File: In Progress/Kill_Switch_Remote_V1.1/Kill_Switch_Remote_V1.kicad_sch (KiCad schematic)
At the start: 56 parts, among them J1 USB_B_Micro, J2 S2B-PH-K-S(LF)(SN), J3 U.FL-R-SMT-1(10), Q2 UMH3N, SW4 AS11CH, U1 ESP32-PICO-MINI-02, U2 CP2102N-A02-GQFN28, U3 LP5912-3.3DRV, U4 MCP73871-2CC-Custom, U5 RFM95W-915S2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

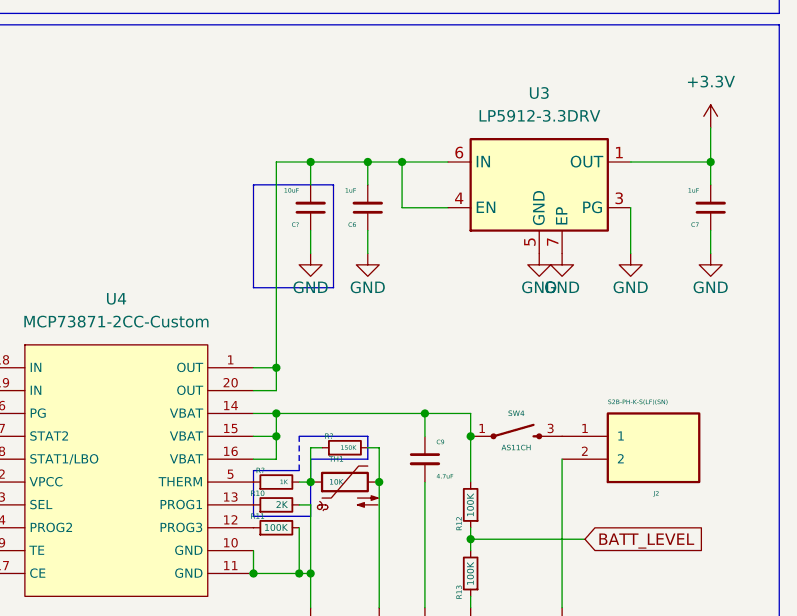
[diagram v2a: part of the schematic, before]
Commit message: changed folder name
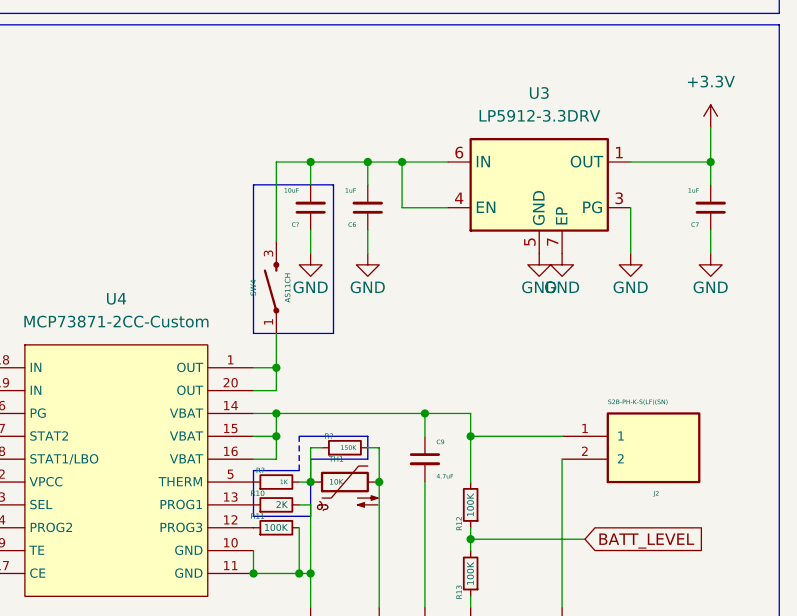
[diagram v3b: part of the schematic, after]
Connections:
- net at J2.1: now also C9.1, R12.2, U4.14 (VBAT), U4.15 (VBAT), U4.16 (VBAT); no longer SW4.3
- net at C6.2, C?.2, U3.4 (EN)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: now also SW4.3; no longer U4.1 (OUT), U4.20 (OUT)
- new net: SW4.1, U4.1 (OUT), U4.20 (OUT)
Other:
- moved on the sheet: SW4
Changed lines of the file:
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@@
   (junction (at 48.26 21.59) (diameter 0) (color 0 0 0 0)
   )
-  (junction (at 248.92 134.62) (diameter 0) (color 0 0 0 0)
-  )
   (junction (at 172.72 127) (diameter 0) (color 0 0 0 0)
   )
@@
   (junction (at 231.14 149.86) (diameter 0) (color 0 0 0 0)
   )
+  (junction (at 248.92 134.62) (diameter 0) (color 0 0 0 0)
+  )
   (junction (at 227.33 127) (diameter 0) (color 0 0 0 0)
   )
@@
     (stroke (width 0) (type default) (color 0 0 0 0))
   )
-  (polyline (pts (xy 233.68 106.68) (xy 233.68 118.11))
+  (polyline (pts (xy 233.68 106.68) (xy 233.68 123.19))
     (stroke (width 0) (type default) (color 0 0 0 0))
   )
@@
     (stroke (width 0) (type default) (color 0 0 0 0))
   )
+  (wire (pts (xy 248.92 134.62) (xy 248.92 139.7))
+    (stroke (width 0) (type default) (color 0 0 0 0))
+  )
   (wire (pts (xy 220.98 59.69) (xy 220.98 60.96))
     (stroke (width 0) (type default) (color 0 0 0 0))
@@
     (stroke (width 0) (type default) (color 0 0 0 0))
   )
-  (polyline (pts (xy 224.79 106.68) (xy 224.79 118.11))
+  (polyline (pts (xy 224.79 106.68) (xy 224.79 123.19))
     (stroke (width 0) (type default) (color 0 0 0 0))
   )
@@
     (stroke (width 0) (type default) (color 0 0 0 0))
   )
-  (wire (pts (xy 248.92 134.62) (xy 248.92 139.7))
-    (stroke (width 0) (type default) (color 0 0 0 0))
-  )
   (wire (pts (xy 179.07 142.24) (xy 179.07 151.13))
     (stroke (width 0) (type default) (color 0 0 0 0))
@@
     (stroke (width 0) (type default) (color 0 0 0 0))
   )
-  (wire (pts (xy 227.33 104.14) (xy 227.33 127))
+  (wire (pts (xy 227.33 104.14) (xy 227.33 113.03))
     (stroke (width 0) (type default) (color 0 0 0 0))
   )
@@
     (stroke (width 0) (type default) (color 0 0 0 0))
   )
+  (wire (pts (xy 248.92 134.62) (xy 259.08 134.62))
+    (stroke (width 0) (type default) (color 0 0 0 0))
+  )
   (wire (pts (xy 83.82 21.59) (xy 83.82 26.67))
     (stroke (width 0) (type default) (color 0 0 0 0))
@@
     (stroke (width 0) (type default) (color 0 0 0 0))
   )
+  (wire (pts (xy 227.33 123.19) (xy 227.33 127))
+    (stroke (width 0) (type default) (color 0 0 0 0))
+  )
   (wire (pts (xy 17.78 68.58) (xy 20.32 68.58))
     (stroke (width 0) (type default) (color 0 0 0 0))
@@
     (stroke (width 0) (type default) (color 0 0 0 0))
   )
-  (polyline (pts (xy 233.68 118.11) (xy 224.79 118.11))
+  (polyline (pts (xy 233.68 123.19) (xy 224.79 123.19))
     (stroke (width 0) (type default) (color 0 0 0 0))
   )
@@
     (pin "1")
   )
-  (symbol (lib_id "Custom:AS11CH") (at 254 134.62 0) (unit 1)
+  (symbol (lib_id "Custom:AS11CH") (at 227.33 118.11 90) (unit 1)
     (in_bom yes) (on_board yes)
-    (property "Reference" "SW4" (id 0) (at 254 132.08 0)
+    (property "Reference" "SW4" (id 0) (at 224.79 118.11 0)
       (effects (font (size 0.6 0.6)))
     )
-    (property "Value" "AS11CH" (id 1) (at 254 135.89 0)
+    (property "Value" "AS11CH" (id 1) (at 228.6 118.11 0)
       (effects (font (size 0.6 0.6)))
     )
-    (property "Footprint" "Custom:AS11CH" (id 2) (at 254 134.62 0)
+    (property "Footprint" "Custom:AS11CH" (id 2) (at 227.33 118.11 0)
       (effects (font (size 1.27 1.27)) (justify bottom) hide)
     )
-    (property "Datasheet" "https://www.nkkswitches.com/pdf/Aslides.pdf" (id 3) (at 254 134.62 0)
+    (property "Datasheet" "https://www.nkkswitches.com/pdf/Aslides.pdf" (id 3) (at 227.33 118.11 0)
       (effects (font (size 1.27 1.27)) hide)
     )
-    (property "Manufacturers Name" "NKK Switches" (id 4) (at 254 134.62 0)
+    (property "Manufacturers Name" "NKK Switches" (id 4) (at 227.33 118.11 0)
       (effects (font (size 1.27 1.27)) hide)
     )
-    (property "Manufacturers Part Number" "AS11CH" (id 5) (at 254 134.62 0)
+    (property "Manufacturers Part Number" "AS11CH" (id 5) (at 227.33 118.11 0)
       (effects (font (size 1.27 1.27)) hide)
     )
-    (property "Digikey Part Number" "360-2728-ND" (id 6) (at 254 134.62 0)
+    (property "Digikey Part Number" "360-2728-ND" (id 6) (at 227.33 118.11 0)
       (effects (font (size 1.27 1.27)) hide)
     )
-    (property "Mouser Part Number" "633-AS11CH " (id 7) (at 254 134.62 0)
+    (property "Mouser Part Number" "633-AS11CH " (id 7) (at 227.33 118.11 0)
       (effects (font (size 1.27 1.27)) hide)
     )
-    (property "LCSC" "-----" (id 8) (at 254 134.62 0)
+    (property "LCSC" "-----" (id 8) (at 227.33 118.11 0)
       (effects (font (size 1.27 1.27)) hide)
     )

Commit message: some minor updates
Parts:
- S1: LCSC ------ -> C2886898; Manufacturers Part Number TL3342F160QG/TR -> TL3342F160QG
- S2, S3: Manufacturer (none) -> E-Switch; Manufacturer's Part Number (none) -> TL3305CF260QG
- U6: LCSC (none) -> C516788; Manufacturer (none) -> Analog Devices Inc./Maxim Integrated; Manufacturer's Part Number (none) -> MAX6817EUT+T
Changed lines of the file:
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@@
+      (effects (font (size 1.27 1.27)) hide)
+    )
+    (property "Manufacturer" " E-Switch" (id 10) (at 29.21 115.57 0)
+      (effects (font (size 1.27 1.27)) hide)
+    )
+    (property "Manufacturer's Part Number" "TL3305CF260QG" (id 11) (at 29.21 115.57 0)
       (effects (font (size 1.27 1.27)) hide)
     )
@@
       (effects (font (size 1.27 1.27)) (justify bottom) hide)
     )
+    (property "LCSC" "C516788" (id 9) (at 48.26 119.38 0)
+      (effects (font (size 1.27 1.27)) hide)
+    )
+    (property "Manufacturer" " Analog Devices Inc./Maxim Integrated" (id 10) (at 48.26 119.38 0)
+      (effects (font (size 1.27 1.27)) hide)
+    )
+    (property "Manufacturer's Part Number" " MAX6817EUT+T" (id 11) (at 48.26 119.38 0)
+      (effects (font (size 1.27 1.27)) hide)
+    )
     (pin "1")
     (pin "2")
@@
       (effects (font (size 1.27 1.27)) hide)
     )
+    (property "Manufacturer" " E-Switch" (id 10) (at 29.21 127 0)
+      (effects (font (size 1.27 1.27)) hide)
+    )
+    (property "Manufacturer's Part Number" "TL3305CF260QG" (id 11) (at 29.21 127 0)
+      (effects (font (size 1.27 1.27)) hide)
+    )
     (pin "1")
     (pin "2")
@@
       (effects (font (size 1.27 1.27)) hide)
     )
-    (property "Manufacturers Part Number" "TL3342F160QG/TR" (id 6) (at 25.4 71.12 0)
+    (property "Manufacturers Part Number" "TL3342F160QG" (id 6) (at 25.4 71.12 0)
       (effects (font (size 1.27 1.27)) hide)
     )
@@
       (effects (font (size 1.27 1.27)) hide)
     )
-    (property "LCSC" "------" (id 9) (at 25.4 71.12 0)
-      (effects (font (size 1.27 1.27)) hide)
-    )
+    (property "LCSC" "C2886898" (id 9) (at 25.4 71.12 0)
+      (effects (font (size 1.27 1.27)) hide)
+    )
